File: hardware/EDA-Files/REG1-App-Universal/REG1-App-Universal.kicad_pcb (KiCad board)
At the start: 2 copper layers, 83 x 34.8 mm, 15 parts, among them J1 Conn_01x06, J10 Conn_01x22, J11 Conn_01x22, J12 Conn_01x22, J13 Conn_01x22, J14 Conn_01x22, J2 Conn_01x06, J3 Conn_01x10, J4 Conn_01x06, J5 Conn_01x10, J6 Conn_01x06, J7 Conn_01x22, J8 Conn_01x22, J9 Conn_01x22

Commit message: REG1-App-Universal V00.02
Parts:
- removed J13: Conn_01x22, Connector_PinHeader_2.54mm:PinHeader_1x22_P2.54mm_Vertical
- moved G*** 54.5 mm to (138.9, 95.8)
- moved J4 2.54 mm to (81.9, 102.9)
- moved J6 2.54 mm to (140.3, 115.6)
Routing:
- net Net-(J2-Pad6): track 9.78 -> 7.99 mm
- net Net-(J1-Pad2): track 8.40 -> 6.77 mm
- net Net-(J2-Pad2): track 7.47 -> 6.40 mm
- net Net-(J2-Pad3): track 7.87 -> 6.79 mm
- net Net-(J1-Pad3): track 7.44 -> 6.37 mm
- net Net-(J1-Pad1): track 8.83 -> 8.03 mm
- net Net-(J2-Pad5): track 8.29 -> 7.59 mm
- net Net-(J1-Pad5): track 6.13 -> 5.57 mm
- net Net-(J1-Pad4): track 6.52 -> 5.97 mm
- net Net-(J2-Pad4): track 7.74 -> 7.19 mm
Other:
- board size 83 x 34.8 mm -> 83 x 32.8 mm
- board text added: "REG1-App-Universal V00.02 by Ing-Dom 2022"
- board text removed: "REG1-App-Universal V00.01"

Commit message: editorial V00.10 of App-Universal
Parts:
- removed J14: Conn_01x22, Connector_PinHeader_2.54mm:PinHeader_1x22_P2.54mm_Vertical
- removed J3: Conn_01x10, Connector_PinHeader_2.54mm:PinHeader_1x10_P2.54mm_Horizontal
- removed J5: Conn_01x10, Connector_PinHeader_2.54mm:PinHeader_1x10_P2.54mm_Vertical
- added J1: REG1_App_Connector, Connector_PinHeader_2.54mm:PinHeader_1x10_P2.54mm_Horizontal, B.Cu at (130.8, 94.3)
- added J2: Conn_01x10, Connector_PinHeader_2.54mm:PinHeader_1x10_P2.54mm_Vertical, B.Cu at (130.2, 97.8)
- added J36: Conn_01x22, Connector_PinHeader_2.54mm:PinHeader_1x22_P2.54mm_Vertical, B.Cu at (84.4, 115.6)
- renumbered J1 to J10, J4 to J11, J2 to J20, J6 to J21, J7 to J30, J8 to J31, J9 to J32, J10 to J33, J11 to J34, J12 to J35
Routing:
- net Net-(J10-Pad5): track 5.57 -> 10.6 mm
- net Net-(J3-Pad8): track 3.73 -> 0.00 mm
- net Net-(J3-Pad6): track 3.73 -> 0.00 mm
- net Net-(J3-Pad3): track 3.73 -> 0.00 mm
- net Net-(J3-Pad10): track 3.73 -> 0.00 mm
- net Net-(J1-Pad8): track 0.00 -> 3.73 mm
- net Net-(J1-Pad6): track 0.00 -> 3.73 mm
- net Net-(J1-Pad3): track 0.00 -> 3.73 mm
- net Net-(J1-Pad10): track 0.00 -> 3.73 mm
- net Net-(J3-Pad9): track 3.73 -> 0.00 mm
- net Net-(J3-Pad7): track 3.73 -> 0.00 mm
- net Net-(J3-Pad5): track 3.73 -> 0.00 mm
- net Net-(J3-Pad4): track 3.73 -> 0.00 mm
- net Net-(J3-Pad2): track 3.73 -> 0.00 mm
- net Net-(J3-Pad1): track 3.73 -> 0.00 mm
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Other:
- board text added: "REG1-App-Universal V00.10 by Ing-Dom 2023"
- board text removed: "REG1-App-Universal V00.02 by Ing-Dom 2022"

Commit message: REG1-App-Universal V00.90
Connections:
- J30 pad 1: Net-(J30-Pad1) -> unconnected-(J30-Pin_1-Pad1)
- J30 pad 10: Net-(J30-Pad10) -> unconnected-(J30-Pin_10-Pad10)
- J30 pad 11: Net-(J30-Pad11) -> unconnected-(J30-Pin_11-Pad11)
- J30 pad 12: Net-(J30-Pad12) -> unconnected-(J30-Pin_12-Pad12)
- J30 pad 13: Net-(J30-Pad13) -> unconnected-(J30-Pin_13-Pad13)
- J30 pad 14: Net-(J30-Pad14) -> unconnected-(J30-Pin_14-Pad14)
- J30 pad 15: Net-(J30-Pad15) -> unconnected-(J30-Pin_15-Pad15)
- J30 pad 16: Net-(J30-Pad16) -> unconnected-(J30-Pin_16-Pad16)
- J30 pad 17: Net-(J30-Pad17) -> unconnected-(J30-Pin_17-Pad17)
- J30 pad 18: Net-(J30-Pad18) -> unconnected-(J30-Pin_18-Pad18)
- J30 pad 19: Net-(J30-Pad19) -> unconnected-(J30-Pin_19-Pad19)
- J30 pad 2: Net-(J30-Pad2) -> unconnected-(J30-Pin_2-Pad2)
- J30 pad 20: Net-(J30-Pad20) -> unconnected-(J30-Pin_20-Pad20)
- J30 pad 21: Net-(J30-Pad21) -> unconnected-(J30-Pin_21-Pad21)
- J30 pad 22: Net-(J30-Pad22) -> unconnected-(J30-Pin_22-Pad22)
- J30 pad 3: Net-(J30-Pad3) -> unconnected-(J30-Pin_3-Pad3)
- J30 pad 4: Net-(J30-Pad4) -> unconnected-(J30-Pin_4-Pad4)
- J30 pad 5: Net-(J30-Pad5) -> unconnected-(J30-Pin_5-Pad5)
- J30 pad 6: Net-(J30-Pad6) -> unconnected-(J30-Pin_6-Pad6)
- J30 pad 7: Net-(J30-Pad7) -> unconnected-(J30-Pin_7-Pad7)
- J30 pad 8: Net-(J30-Pad8) -> unconnected-(J30-Pin_8-Pad8)
- J30 pad 9: Net-(J30-Pad9) -> unconnected-(J30-Pin_9-Pad9)
- J31 pad 1: Net-(J31-Pad1) -> unconnected-(J31-Pin_1-Pad1)
- J31 pad 10: Net-(J31-Pad10) -> unconnected-(J31-Pin_10-Pad10)
- J31 pad 11: Net-(J31-Pad11) -> unconnected-(J31-Pin_11-Pad11)
- J31 pad 12: Net-(J31-Pad12) -> unconnected-(J31-Pin_12-Pad12)
- J31 pad 13: Net-(J31-Pad13) -> unconnected-(J31-Pin_13-Pad13)
- J31 pad 14: Net-(J31-Pad14) -> unconnected-(J31-Pin_14-Pad14)
- J31 pad 15: Net-(J31-Pad15) -> unconnected-(J31-Pin_15-Pad15)
- J31 pad 16: Net-(J31-Pad16) -> unconnected-(J31-Pin_16-Pad16)
- J31 pad 17: Net-(J31-Pad17) -> unconnected-(J31-Pin_17-Pad17)
- J31 pad 18: Net-(J31-Pad18) -> unconnected-(J31-Pin_18-Pad18)
- J31 pad 19: Net-(J31-Pad19) -> unconnected-(J31-Pin_19-Pad19)
- J31 pad 2: Net-(J31-Pad2) -> unconnected-(J31-Pin_2-Pad2)
- J31 pad 20: Net-(J31-Pad20) -> unconnected-(J31-Pin_20-Pad20)
- J31 pad 21: Net-(J31-Pad21) -> unconnected-(J31-Pin_21-Pad21)
- J31 pad 22: Net-(J31-Pad22) -> unconnected-(J31-Pin_22-Pad22)
- J31 pad 3: Net-(J31-Pad3) -> unconnected-(J31-Pin_3-Pad3)
- J31 pad 4: Net-(J31-Pad4) -> unconnected-(J31-Pin_4-Pad4)
- J31 pad 5: Net-(J31-Pad5) -> unconnected-(J31-Pin_5-Pad5)
- J31 pad 6: Net-(J31-Pad6) -> unconnected-(J31-Pin_6-Pad6)
- J31 pad 7: Net-(J31-Pad7) -> unconnected-(J31-Pin_7-Pad7)
- J31 pad 8: Net-(J31-Pad8) -> unconnected-(J31-Pin_8-Pad8)
- J31 pad 9: Net-(J31-Pad9) -> unconnected-(J31-Pin_9-Pad9)
- J32 pad 1: Net-(J32-Pad1) -> unconnected-(J32-Pin_1-Pad1)
- J32 pad 10: Net-(J32-Pad10) -> unconnected-(J32-Pin_10-Pad10)
- J32 pad 11: Net-(J32-Pad11) -> unconnected-(J32-Pin_11-Pad11)
- J32 pad 12: Net-(J32-Pad12) -> unconnected-(J32-Pin_12-Pad12)
- J32 pad 13: Net-(J32-Pad13) -> unconnected-(J32-Pin_13-Pad13)
- J32 pad 14: Net-(J32-Pad14) -> unconnected-(J32-Pin_14-Pad14)
- J32 pad 15: Net-(J32-Pad15) -> unconnected-(J32-Pin_15-Pad15)
- J32 pad 16: Net-(J32-Pad16) -> unconnected-(J32-Pin_16-Pad16)
- J32 pad 17: Net-(J32-Pad17) -> unconnected-(J32-Pin_17-Pad17)
- J32 pad 18: Net-(J32-Pad18) -> unconnected-(J32-Pin_18-Pad18)
- J32 pad 19: Net-(J32-Pad19) -> unconnected-(J32-Pin_19-Pad19)
- J32 pad 2: Net-(J32-Pad2) -> unconnected-(J32-Pin_2-Pad2)
- J32 pad 20: Net-(J32-Pad20) -> unconnected-(J32-Pin_20-Pad20)
- J32 pad 21: Net-(J32-Pad21) -> unconnected-(J32-Pin_21-Pad21)
- J32 pad 22: Net-(J32-Pad22) -> unconnected-(J32-Pin_22-Pad22)
- J32 pad 3: Net-(J32-Pad3) -> unconnected-(J32-Pin_3-Pad3)
- J32 pad 4: Net-(J32-Pad4) -> unconnected-(J32-Pin_4-Pad4)
- J32 pad 5: Net-(J32-Pad5) -> unconnected-(J32-Pin_5-Pad5)
- J32 pad 6: Net-(J32-Pad6) -> unconnected-(J32-Pin_6-Pad6)
- J32 pad 7: Net-(J32-Pad7) -> unconnected-(J32-Pin_7-Pad7)
- J32 pad 8: Net-(J32-Pad8) -> unconnected-(J32-Pin_8-Pad8)
- J32 pad 9: Net-(J32-Pad9) -> unconnected-(J32-Pin_9-Pad9)
- J33 pad 1: Net-(J33-Pad1) -> unconnected-(J33-Pin_1-Pad1)
- J33 pad 10: Net-(J33-Pad10) -> unconnected-(J33-Pin_10-Pad10)
- J33 pad 11: Net-(J33-Pad11) -> unconnected-(J33-Pin_11-Pad11)
- J33 pad 12: Net-(J33-Pad12) -> unconnected-(J33-Pin_12-Pad12)
- J33 pad 13: Net-(J33-Pad13) -> unconnected-(J33-Pin_13-Pad13)
- J33 pad 14: Net-(J33-Pad14) -> unconnected-(J33-Pin_14-Pad14)
- J33 pad 15: Net-(J33-Pad15) -> unconnected-(J33-Pin_15-Pad15)
- J33 pad 16: Net-(J33-Pad16) -> unconnected-(J33-Pin_16-Pad16)
- J33 pad 17: Net-(J33-Pad17) -> unconnected-(J33-Pin_17-Pad17)
- J33 pad 18: Net-(J33-Pad18) -> unconnected-(J33-Pin_18-Pad18)
- J33 pad 19: Net-(J33-Pad19) -> unconnected-(J33-Pin_19-Pad19)
- J33 pad 2: Net-(J33-Pad2) -> unconnected-(J33-Pin_2-Pad2)
- J33 pad 20: Net-(J33-Pad20) -> unconnected-(J33-Pin_20-Pad20)
- J33 pad 21: Net-(J33-Pad21) -> unconnected-(J33-Pin_21-Pad21)
- J33 pad 22: Net-(J33-Pad22) -> unconnected-(J33-Pin_22-Pad22)
- J33 pad 3: Net-(J33-Pad3) -> unconnected-(J33-Pin_3-Pad3)
- J33 pad 4: Net-(J33-Pad4) -> unconnected-(J33-Pin_4-Pad4)
- J33 pad 5: Net-(J33-Pad5) -> unconnected-(J33-Pin_5-Pad5)
- J33 pad 6: Net-(J33-Pad6) -> unconnected-(J33-Pin_6-Pad6)
- J33 pad 7: Net-(J33-Pad7) -> unconnected-(J33-Pin_7-Pad7)
- J33 pad 8: Net-(J33-Pad8) -> unconnected-(J33-Pin_8-Pad8)
- J33 pad 9: Net-(J33-Pad9) -> unconnected-(J33-Pin_9-Pad9)
- J34 pad 1: Net-(J34-Pad1) -> unconnected-(J34-Pin_1-Pad1)
- J34 pad 10: Net-(J34-Pad10) -> unconnected-(J34-Pin_10-Pad10)
- J34 pad 11: Net-(J34-Pad11) -> unconnected-(J34-Pin_11-Pad11)
- J34 pad 12: Net-(J34-Pad12) -> unconnected-(J34-Pin_12-Pad12)
- J34 pad 13: Net-(J34-Pad13) -> unconnected-(J34-Pin_13-Pad13)
- J34 pad 14: Net-(J34-Pad14) -> unconnected-(J34-Pin_14-Pad14)
- J34 pad 15: Net-(J34-Pad15) -> unconnected-(J34-Pin_15-Pad15)
- J34 pad 16: Net-(J34-Pad16) -> unconnected-(J34-Pin_16-Pad16)
- J34 pad 17: Net-(J34-Pad17) -> unconnected-(J34-Pin_17-Pad17)
- J34 pad 18: Net-(J34-Pad18) -> unconnected-(J34-Pin_18-Pad18)
- J34 pad 19: Net-(J34-Pad19) -> unconnected-(J34-Pin_19-Pad19)
- J34 pad 2: Net-(J34-Pad2) -> unconnected-(J34-Pin_2-Pad2)
- J34 pad 20: Net-(J34-Pad20) -> unconnected-(J34-Pin_20-Pad20)
- J34 pad 21: Net-(J34-Pad21) -> unconnected-(J34-Pin_21-Pad21)
- J34 pad 22: Net-(J34-Pad22) -> unconnected-(J34-Pin_22-Pad22)
- J34 pad 3: Net-(J34-Pad3) -> unconnected-(J34-Pin_3-Pad3)
- J34 pad 4: Net-(J34-Pad4) -> unconnected-(J34-Pin_4-Pad4)
- J34 pad 5: Net-(J34-Pad5) -> unconnected-(J34-Pin_5-Pad5)
- J34 pad 6: Net-(J34-Pad6) -> unconnected-(J34-Pin_6-Pad6)
- J34 pad 7: Net-(J34-Pad7) -> unconnected-(J34-Pin_7-Pad7)
- J34 pad 8: Net-(J34-Pad8) -> unconnected-(J34-Pin_8-Pad8)
- J34 pad 9: Net-(J34-Pad9) -> unconnected-(J34-Pin_9-Pad9)
- J35 pad 1: Net-(J35-Pad1) -> unconnected-(J35-Pin_1-Pad1)
- J35 pad 10: Net-(J35-Pad10) -> unconnected-(J35-Pin_10-Pad10)
- J35 pad 11: Net-(J35-Pad11) -> unconnected-(J35-Pin_11-Pad11)
- J35 pad 12: Net-(J35-Pad12) -> unconnected-(J35-Pin_12-Pad12)
- J35 pad 13: Net-(J35-Pad13) -> unconnected-(J35-Pin_13-Pad13)
- J35 pad 14: Net-(J35-Pad14) -> unconnected-(J35-Pin_14-Pad14)
- J35 pad 15: Net-(J35-Pad15) -> unconnected-(J35-Pin_15-Pad15)
- J35 pad 16: Net-(J35-Pad16) -> unconnected-(J35-Pin_16-Pad16)
- J35 pad 17: Net-(J35-Pad17) -> unconnected-(J35-Pin_17-Pad17)
- J35 pad 18: Net-(J35-Pad18) -> unconnected-(J35-Pin_18-Pad18)
- J35 pad 19: Net-(J35-Pad19) -> unconnected-(J35-Pin_19-Pad19)
- J35 pad 2: Net-(J35-Pad2) -> unconnected-(J35-Pin_2-Pad2)
- J35 pad 20: Net-(J35-Pad20) -> unconnected-(J35-Pin_20-Pad20)
- J35 pad 21: Net-(J35-Pad21) -> unconnected-(J35-Pin_21-Pad21)
- J35 pad 22: Net-(J35-Pad22) -> unconnected-(J35-Pin_22-Pad22)
- J35 pad 3: Net-(J35-Pad3) -> unconnected-(J35-Pin_3-Pad3)
- J35 pad 4: Net-(J35-Pad4) -> unconnected-(J35-Pin_4-Pad4)
- J35 pad 5: Net-(J35-Pad5) -> unconnected-(J35-Pin_5-Pad5)
- J35 pad 6: Net-(J35-Pad6) -> unconnected-(J35-Pin_6-Pad6)
- J35 pad 7: Net-(J35-Pad7) -> unconnected-(J35-Pin_7-Pad7)
- J35 pad 8: Net-(J35-Pad8) -> unconnected-(J35-Pin_8-Pad8)
- J35 pad 9: Net-(J35-Pad9) -> unconnected-(J35-Pin_9-Pad9)
- J36 pad 1: Net-(J36-Pad1) -> unconnected-(J36-Pin_1-Pad1)
- J36 pad 10: Net-(J36-Pad10) -> unconnected-(J36-Pin_10-Pad10)
- J36 pad 11: Net-(J36-Pad11) -> unconnected-(J36-Pin_11-Pad11)
- J36 pad 12: Net-(J36-Pad12) -> unconnected-(J36-Pin_12-Pad12)
- J36 pad 13: Net-(J36-Pad13) -> unconnected-(J36-Pin_13-Pad13)
- J36 pad 14: Net-(J36-Pad14) -> unconnected-(J36-Pin_14-Pad14)
- J36 pad 15: Net-(J36-Pad15) -> unconnected-(J36-Pin_15-Pad15)
- J36 pad 16: Net-(J36-Pad16) -> unconnected-(J36-Pin_16-Pad16)
- J36 pad 17: Net-(J36-Pad17) -> unconnected-(J36-Pin_17-Pad17)
- J36 pad 18: Net-(J36-Pad18) -> unconnected-(J36-Pin_18-Pad18)
- J36 pad 19: Net-(J36-Pad19) -> unconnected-(J36-Pin_19-Pad19)
- J36 pad 2: Net-(J36-Pad2) -> unconnected-(J36-Pin_2-Pad2)
- J36 pad 20: Net-(J36-Pad20) -> unconnected-(J36-Pin_20-Pad20)
- J36 pad 21: Net-(J36-Pad21) -> unconnected-(J36-Pin_21-Pad21)
- J36 pad 22: Net-(J36-Pad22) -> unconnected-(J36-Pin_22-Pad22)
- J36 pad 3: Net-(J36-Pad3) -> unconnected-(J36-Pin_3-Pad3)
- J36 pad 4: Net-(J36-Pad4) -> unconnected-(J36-Pin_4-Pad4)
- J36 pad 5: Net-(J36-Pad5) -> unconnected-(J36-Pin_5-Pad5)
- J36 pad 6: Net-(J36-Pad6) -> unconnected-(J36-Pin_6-Pad6)
- J36 pad 7: Net-(J36-Pad7) -> unconnected-(J36-Pin_7-Pad7)
- J36 pad 8: Net-(J36-Pad8) -> unconnected-(J36-Pin_8-Pad8)
- J36 pad 9: Net-(J36-Pad9) -> unconnected-(J36-Pin_9-Pad9)
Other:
- outline, holes or cut-outs redrawn
- net class Default removed
- rule pad_to_mask_clearance: 0.051 -> 0.038
- board text added: "0,2mm Spacing to Case"
- board text added: "REG1-App-Universal V00.90 by Ing-Dom 2023"
- board text removed: "REG1-App-Universal V00.10 by Ing-Dom 2023"

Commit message: REG1-App-Universal_V01.00
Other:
- board text added: "REG1-App-Universal V01.00 (c) Ing-Dom, 2023"
- board text removed: "REG1-App-Universal V00.90 by Ing-Dom 2023"
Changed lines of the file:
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@@
   (paper "A4")
   (title_block
-    (date "2023-10-14")
-    (rev "V00.90")
+    (date "2023-10-15")
+    (rev "V01.00")
   )
   (layers
@@
       (hpglpendiameter 15.000000)
       (dxfpolygonmode true)
-      (dxfimperialunits true)
+      (dxfimperialunits false)
       (dxfusepcbnewfont true)
       (psnegative false)
@@
       (drillshape 0)
       (scaleselection 1)
-      (outputdirectory "REG1-App-Universal_gerbers_V00.90/")
+      (outputdirectory "REG1-App-Universal_gerbers_V01.00/")
     )
   )
@@
     (descr "Generic Phoenix Contact connector footprint for: MC_1,5/6-G-3.5; number of pins: 06; pin pitch: 3.50mm; Angled || order number: 1844252 8A 160V")
     (tags "phoenix_contact connector MC_01x06_G_3.5mm")
-    (property "Sheetfile" "D:/Data/Eigene Dokumente/Projekte/EIB/OpenKNX/OpenKNX-Repos/_REG1/OpenKNX-REG1/hardware/EDA-Files/REG1-App-Universal/REG1-App-Universal.sch")
+    (property "Sheetfile" "REG1-App-Universal.kicad_sch")
     (property "Sheetname" "")
     (property "ki_description" "Generic connector, single row, 01x06, script generated (kicad-library-utils/schlib/autogen/connector/)")
@@
     (fp_line (start 19.95 8) (end 19.95 -1.2)
       (stroke (width 0.1) (type solid)) (layer "F.Fab"))
-    (pad "1" thru_hole roundrect (at 0 0 270) (size 1.8 3.6) (drill 1.2) (layers "*.Cu" "*.Mask") (roundrect_rratio 0.138889)
+    (pad "1" thru_hole roundrect (at 0 0 270) (size 1.8 3.6) (drill 1.2) (layers "*.Cu" "*.Mask") (roundrect_rratio 0.1388888889)
       (net 16 "Net-(J10-Pin_1)") (pinfunction "Pin_1") (pintype "passive"))
     (pad "2" thru_hole oval (at 3.5 0 270) (size 1.8 3.6) (drill 1.2) (layers "*.Cu" "*.Mask")
@@
     (descr "Generic Phoenix Contact connector footprint for: MC_1,5/6-G-3.5; number of pins: 06; pin pitch: 3.50mm; Angled || order number: 1844252 8A 160V")
     (tags "phoenix_contact connector MC_01x06_G_3.5mm")
-    (property "Sheetfile" "D:/Data/Eigene Dokumente/Projekte/EIB/OpenKNX/OpenKNX-Repos/_REG1/OpenKNX-REG1/hardware/EDA-Files/REG1-App-Universal/REG1-App-Universal.sch")
+    (property "Sheetfile" "REG1-App-Universal.kicad_sch")
     (property "Sheetname" "")
     (property "ki_description" "Generic connector, single row, 01x06, script generated (kicad-library-utils/schlib/autogen/connector/)")
@@
     (fp_line (start 19.95 8) (end 19.95 -1.2)
       (stroke (width 0.1) (type solid)) (layer "F.Fab"))
-    (pad "1" thru_hole roundrect (at 0 0 90) (size 1.8 3.6) (drill 1.2) (layers "*.Cu" "*.Mask") (roundrect_rratio 0.138889)
+    (pad "1" thru_hole roundrect (at 0 0 90) (size 1.8 3.6) (drill 1.2) (layers "*.Cu" "*.Mask") (roundrect_rratio 0.1388888889)
       (net 22 "Net-(J20-Pin_1)") (pinfunction "Pin_1") (pintype "passive"))
     (pad "2" thru_hole oval (at 3.5 0 90) (size 1.8 3.6) (drill 1.2) (layers "*.Cu" "*.Mask")
@@
     (descr "Through hole straight pin header, 1x06, 2.54mm pitch, single row")
     (tags "Through hole pin header THT 1x06 2.54mm single row")
-    (property "Sheetfile" "D:/Data/Eigene Dokumente/Projekte/EIB/OpenKNX/OpenKNX-Repos/_REG1/OpenKNX-REG1/hardware/EDA-Files/REG1-App-Universal/REG1-App-Universal.sch")
+    (property "Sheetfile" "REG1-App-Universal.kicad_sch")
     (property "Sheetname" "")
     (property "ki_description" "Generic connector, single row, 01x06, script generated (kicad-library-utils/schlib/autogen/connector/)")
@@
     (descr "Through hole straight pin header, 1x06, 2.54mm pitch, single row")
     (tags "Through hole pin header THT 1x06 2.54mm single row")
-    (property "Sheetfile" "D:/Data/Eigene Dokumente/Projekte/EIB/OpenKNX/OpenKNX-Repos/_REG1/OpenKNX-REG1/hardware/EDA-Files/REG1-App-Universal/REG1-App-Universal.sch")
+    (property "Sheetfile" "REG1-App-Universal.kicad_sch")
     (property "Sheetname" "")
     (property "ki_description" "Generic connector, single row, 01x06, script generated (kicad-library-utils/schlib/autogen/connector/)")
@@
     (descr "Through hole straight pin header, 1x22, 2.54mm pitch, single row")
     (tags "Through hole pin header THT 1x22 2.54mm single row")
-    (property "Sheetfile" "D:/Data/Eigene Dokumente/Projekte/EIB/OpenKNX/OpenKNX-Repos/_REG1/OpenKNX-REG1/hardware/EDA-Files/REG1-App-Universal/REG1-App-Universal.sch")
+    (property "Sheetfile" "REG1-App-Universal.kicad_sch")
     (property "Sheetname" "")
     (property "ki_description" "Generic connector, single row, 01x22, script generated (kicad-library-utils/schlib/autogen/connector/)")
@@
     (descr "Through hole straight pin header, 1x22, 2.54mm pitch, single row")
     (tags "Through hole pin header THT 1x22 2.54mm single row")
-    (property "Sheetfile" "D:/Data/Eigene Dokumente/Projekte/EIB/OpenKNX/OpenKNX-Repos/_REG1/OpenKNX-REG1/hardware/EDA-Files/REG1-App-Universal/REG1-App-Universal.sch")
+    (property "Sheetfile" "REG1-App-Universal.kicad_sch")
     (property "Sheetname" "")
     (property "ki_description" "Generic connector, single row, 01x22, script generated (kicad-library-utils/schlib/autogen/connector/)")
@@
     (descr "Through hole straight pin header, 1x22, 2.54mm pitch, single row")
     (tags "Through hole pin header THT 1x22 2.54mm single row")
-    (property "Sheetfile" "D:/Data/Eigene Dokumente/Projekte/EIB/OpenKNX/OpenKNX-Repos/_REG1/OpenKNX-REG1/hardware/EDA-Files/REG1-App-Universal/REG1-App-Universal.sch")
+    (property "Sheetfile" "REG1-App-Universal.kicad_sch")
     (property "Sheetname" "")
     (property "ki_description" "Generic connector, single row, 01x22, script generated (kicad-library-utils/schlib/autogen/connector/)")
@@
     (descr "Through hole straight pin header, 1x22, 2.54mm pitch, single row")
     (tags "Through hole pin header THT 1x22 2.54mm single row")
-    (property "Sheetfile" "D:/Data/Eigene Dokumente/Projekte/EIB/OpenKNX/OpenKNX-Repos/_REG1/OpenKNX-REG1/hardware/EDA-Files/REG1-App-Universal/REG1-App-Universal.sch")
+    (property "Sheetfile" "REG1-App-Universal.kicad_sch")
     (property "Sheetname" "")
     (property "ki_description" "Generic connector, single row, 01x22, script generated (kicad-library-utils/schlib/autogen/connector/)")
@@
     (descr "Through hole straight pin header, 1x22, 2.54mm pitch, single row")
     (tags "Through hole pin header THT 1x22 2.54mm single row")
-    (property "Sheetfile" "D:/Data/Eigene Dokumente/Projekte/EIB/OpenKNX/OpenKNX-Repos/_REG1/OpenKNX-REG1/hardware/EDA-Files/REG1-App-Universal/REG1-App-Universal.sch")
+    (property "Sheetfile" "REG1-App-Universal.kicad_sch")
     (property "Sheetname" "")
     (property "ki_description" "Generic connector, single row, 01x22, script generated (kicad-library-utils/schlib/autogen/connector/)")
@@
     (descr "Through hole straight pin header, 1x22, 2.54mm pitch, single row")
     (tags "Through hole pin header THT 1x22 2.54mm single row")
-    (property "Sheetfile" "D:/Data/Eigene Dokumente/Projekte/EIB/OpenKNX/OpenKNX-Repos/_REG1/OpenKNX-REG1/hardware/EDA-Files/REG1-App-Universal/REG1-App-Universal.sch")
+    (property "Sheetfile" "REG1-App-Universal.kicad_sch")
     (property "Sheetname" "")
     (property "ki_description" "Generic connector, single row, 01x22, script generated (kicad-library-utils/schlib/autogen/connector/)")
@@
     (descr "Through hole angled pin header, 1x10, 2.54mm pitch, 6mm pin length, single row")
     (tags "Through hole angled pin header THT 1x10 2.54mm single row")
-    (property "Sheetfile" "D:/Data/Eigene Dokumente/Projekte/EIB/OpenKNX/OpenKNX-Repos/_REG1/OpenKNX-REG1/hardware/EDA-Files/REG1-App-Universal/REG1-App-Universal.sch")
+    (property "Sheetfile" "REG1-App-Universal.kicad_sch")
     (property "Sheetname" "")
     (attr through_hole)
@@
     (descr "Through hole straight pin header, 1x10, 2.54mm pitch, single row")
     (tags "Through hole pin header THT 1x10 2.54mm single row")
-    (property "Sheetfile" "D:/Data/Eigene Dokumente/Projekte/EIB/OpenKNX/OpenKNX-Repos/_REG1/OpenKNX-REG1/hardware/EDA-Files/REG1-App-Universal/REG1-App-Universal.sch")
+    (property "Sheetfile" "REG1-App-Universal.kicad_sch")
     (property "Sheetname" "")
     (property "ki_description" "Generic connector, single row, 01x10, script generated (kicad-library-utils/schlib/autogen/connector/)")
@@
     (descr "Through hole straight pin header, 1x22, 2.54mm pitch, single row")
     (tags "Through hole pin header THT 1x22 2.54mm single row")
-    (property "Sheetfile" "D:/Data/Eigene Dokumente/Projekte/EIB/OpenKNX/OpenKNX-Repos/_REG1/OpenKNX-REG1/hardware/EDA-Files/REG1-App-Universal/REG1-App-Universal.sch")
+    (property "Sheetfile" "REG1-App-Universal.kicad_sch")
     (property "Sheetname" "")
     (property "ki_description" "Generic connector, single row, 01x22, script generated (kicad-library-utils/schlib/autogen/connector/)")
@@
   (gr_line (start 140.9 90.1) (end 140.9 92.4)
     (stroke (width 0.05) (type solid)) (layer "Edge.Cuts"))
-  (gr_text "REG1-App-Universal\nV00.90 by Ing-Dom 2023" (at 83.4 95.1) (layer "F.SilkS")
+  (gr_text "REG1-App-Universal V01.00\n(c) Ing-Dom, 2023" (at 83.4 95.1) (layer "F.SilkS")
     (effects (font (size 1 1) (thickness 0.15)) (justify left))
   )

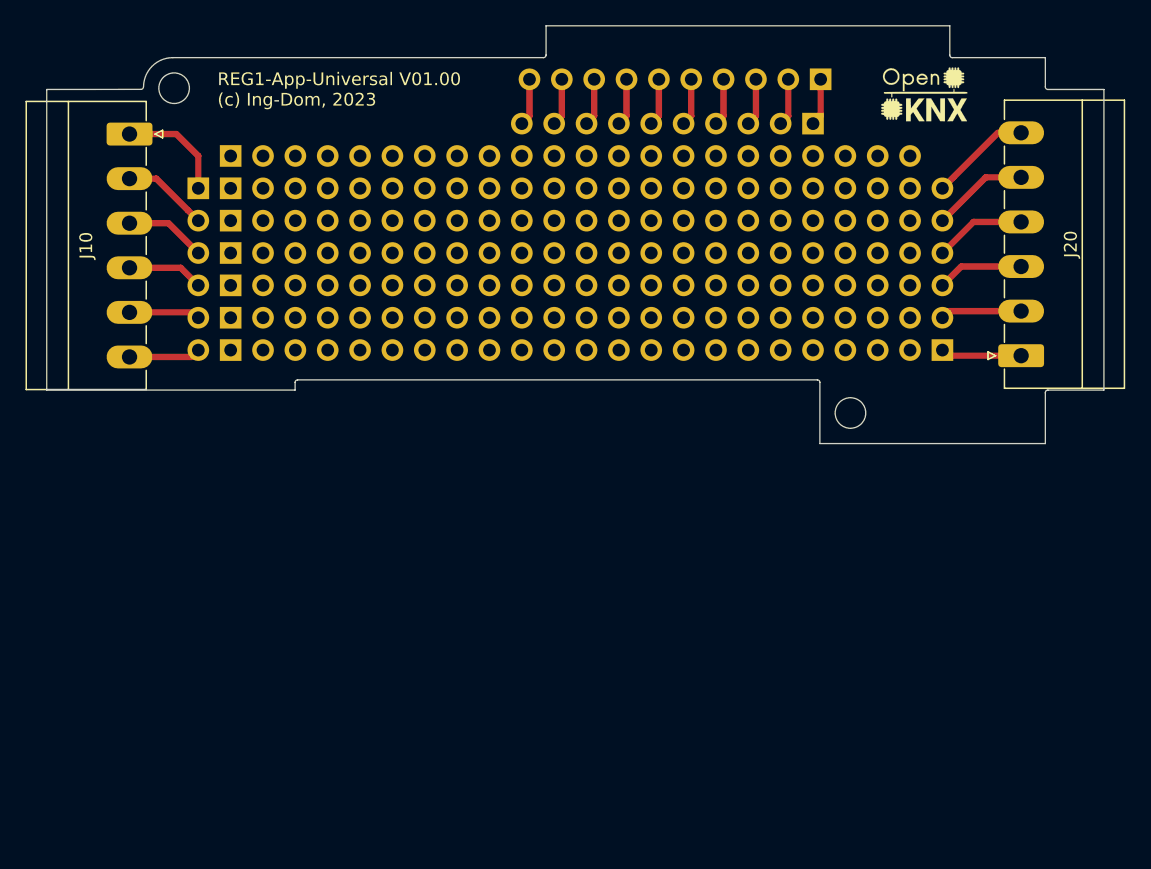
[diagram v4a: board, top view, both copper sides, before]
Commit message: REG1-App-Universal - editorial rework V01.10
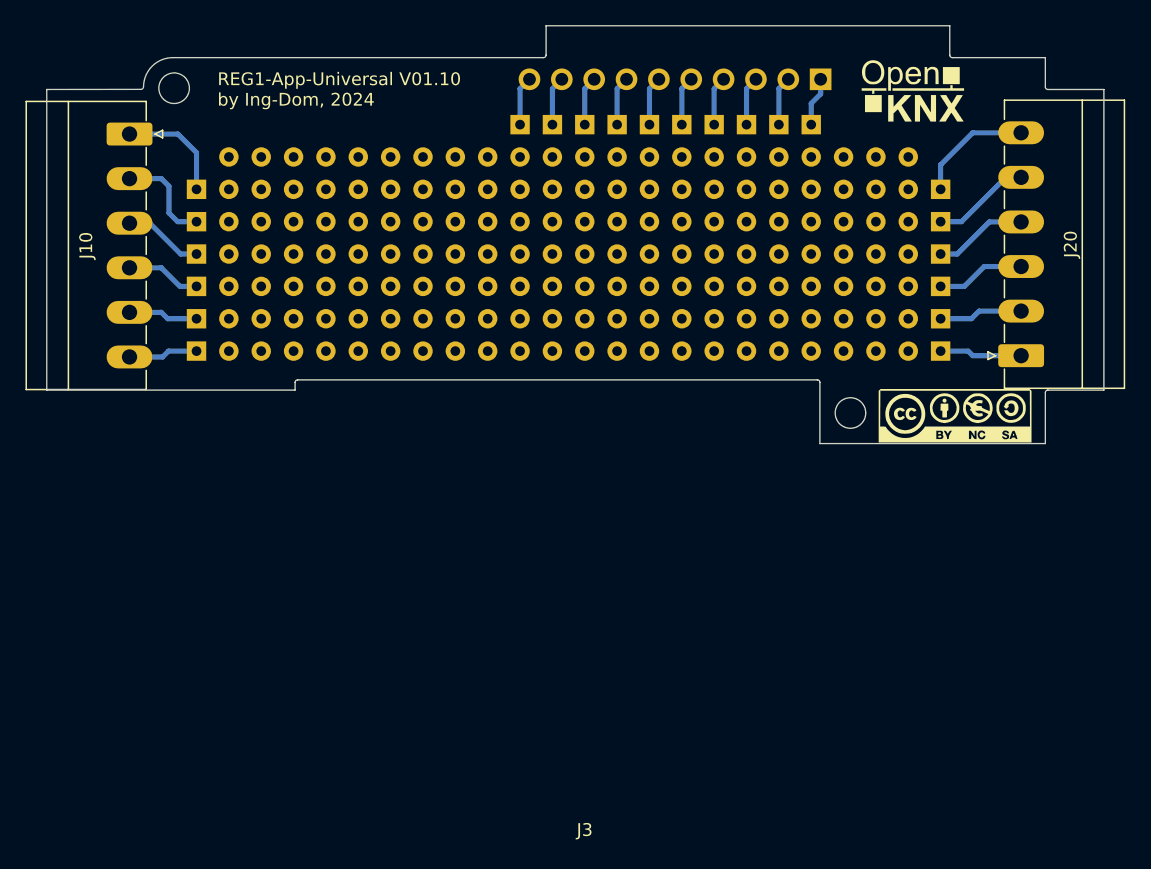
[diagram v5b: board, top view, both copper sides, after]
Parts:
- removed G***: LOGO, OpenKNX:OpenKNX_Logo_07x05
- removed J11, J21: Conn_01x06, Connector_PinHeader_2.54mm:PinHeader_1x06_P2.54mm_Vertical
- removed J2: Conn_01x10, Connector_PinHeader_2.54mm:PinHeader_1x10_P2.54mm_Vertical
- removed J30, J31, J32, J33, J34, J35, J36: Conn_01x22, Connector_PinHeader_2.54mm:PinHeader_1x22_P2.54mm_Vertical
- added G*: LOGO, OpenKNX:CC-BY-NY-SA_12x4, F.Cu at (141.3, 120.7)
- added G*: LOGO, OpenKNX:OpenKNX_Logo_10x10, F.Cu at (138.0, 95.2)
- added J3: REG1_App_Breadboard, OpenKNX:REG1_App_Breadboard, F.Cu at (112.2, 153.7)
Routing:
- net Net-(J10-Pin_5): track 10.6 -> 5.47 mm
- net Net-(J20-Pin_6): track 7.99 -> 9.28 mm
- net Net-(J10-Pin_2): track 6.77 -> 7.89 mm
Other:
- board text added: "REG1-App-Universal V01.10 by Ing-Dom, 2024"
- board text removed: "REG1-App-Universal V01.00 (c) Ing-Dom, 2023"
